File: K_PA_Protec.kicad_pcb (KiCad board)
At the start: 2 copper layers, 102.5 x 75 mm, 89 parts, among them IC1 MCP23017_SO, J1 IDC 10 Straight, J10 MH2, J11 MH3, J12 MH4, J13 MH5, J14 MH6, J2 Molex KK 4, J3 IDC 10 Straight, J4 Molex KK 2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

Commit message: routing, first stage
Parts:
- added G***: LOGO, Mod:Fcu, F.Cu at (115.0, 88.3)
- moved C15 10.6 mm to (88.5, 111.0)
- moved C24 9.96 mm to (127.5, 112.5), turned to -90 degrees
- moved SW1 9.67 mm to (147.8, 116.0), turned to 90 degrees
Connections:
- J2 pad 3: Net-(J2-Pad3) -> Net-(SW1-PadS2)
- SW1 pad S1: Net-(J2-Pad3) -> GND
- SW1 pad S2: GND -> Net-(SW1-PadS2)
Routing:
- net GND: track 0.00 -> 38.9 mm
- net Net-(SW1-PadS2): track 0.00 -> 34.8 mm
- net +12V: track 0.00 -> 24.9 mm
- net Net-(J7-Pad1): track 0.00 -> 13.8 mm
- net +15V: track 0.00 -> 13.4 mm
- net Net-(C15-Pad1): track 0.00 -> 12.4 mm
- net Net-(SW1-Pad2B): track 0.00 -> 7.74 mm
- net Net-(SW1-Pad2A): track 0.00 -> 4.67 mm
- net Net-(L3-Pad1): track 0.00 -> 4.35 mm
- net Net-(L1-Pad1): track 0.00 -> 4.15 mm
- added copper zone on F.Cu, net GND

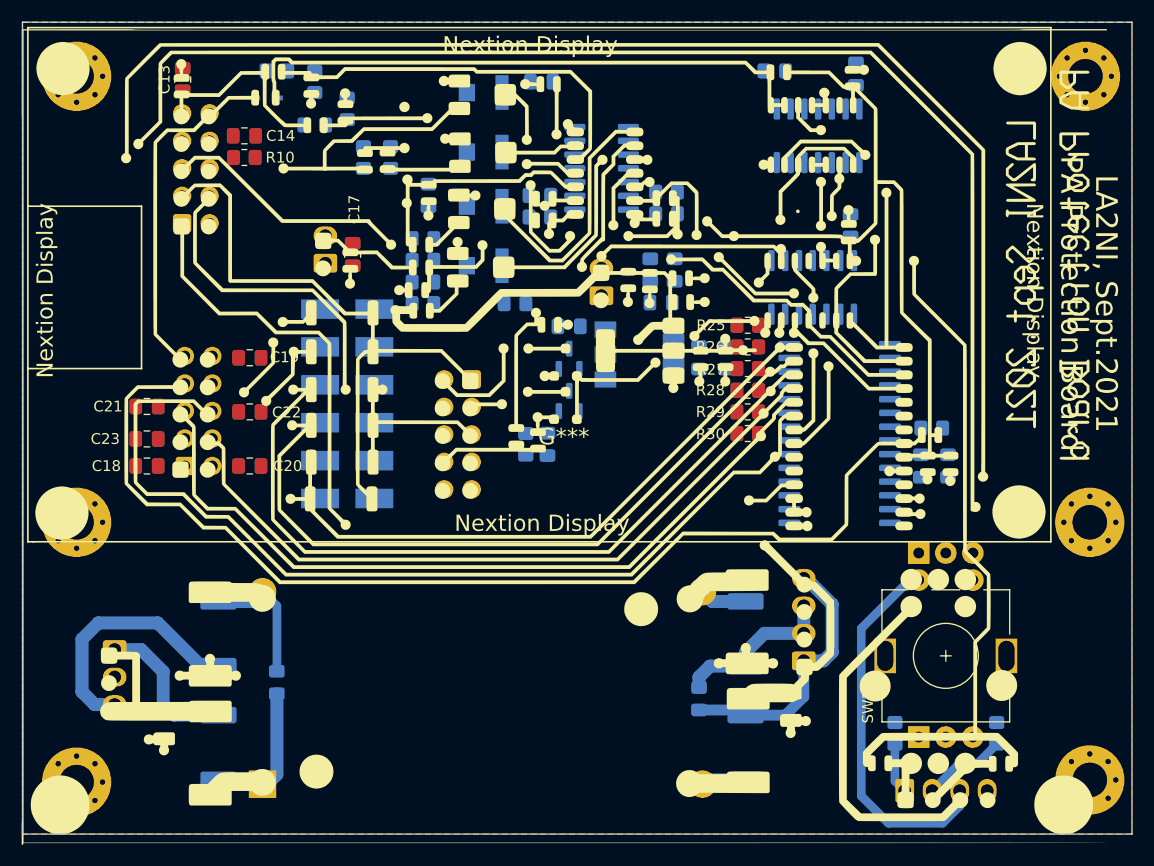
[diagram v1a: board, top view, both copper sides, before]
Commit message: routing completed, some minor changes expected
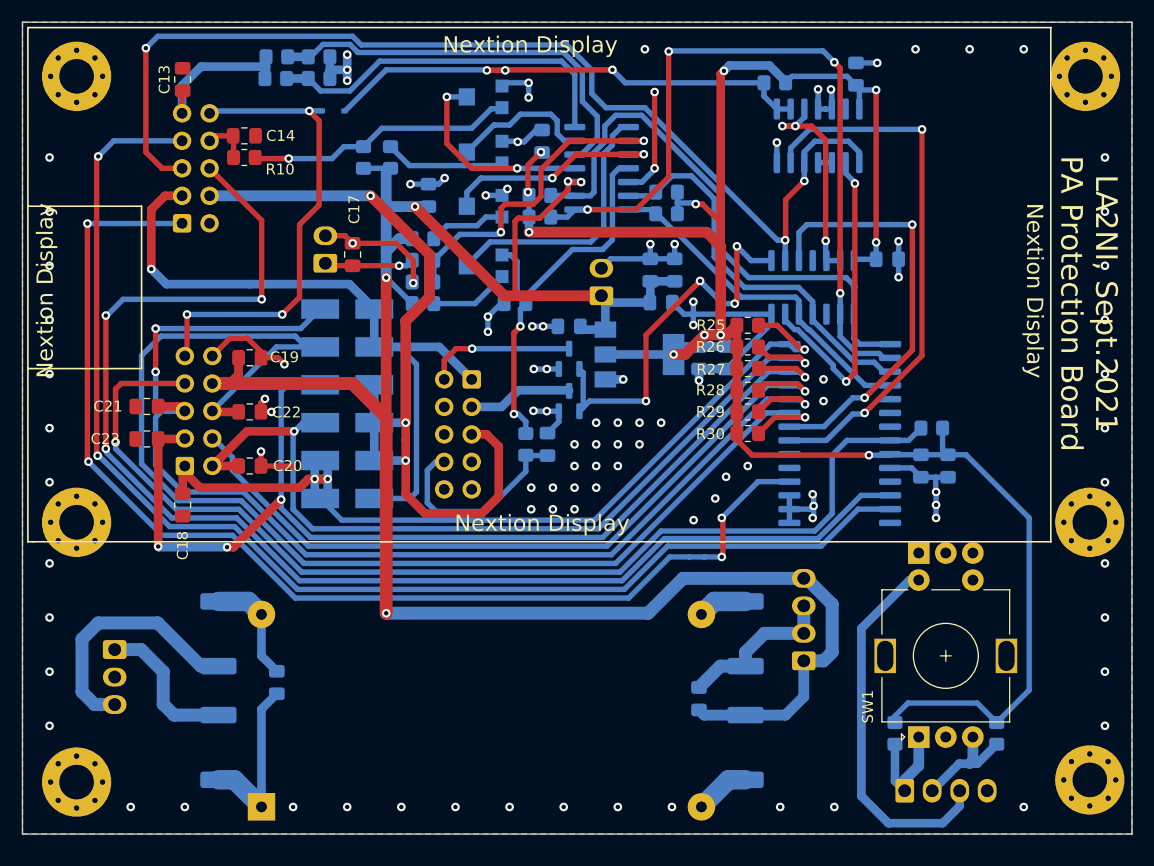
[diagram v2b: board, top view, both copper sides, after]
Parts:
- removed G***: LOGO, Mod:Fcu
- moved D1 6.12 mm to (93.7, 58.2)
- moved R11 5.61 mm to (88.4, 55.2)
- moved C2 5.50 mm to (113.0, 61.0), turned to 90 degrees
- moved C18 4.88 mm to (79.8, 94.6), turned to 90 degrees
- moved C9 4.60 mm to (144.9, 71.9), turned to 180 degrees
- moved R18 3.82 mm to (92.4, 55.2), turned to 180 degrees
- moved R22 2.33 mm to (92.4, 53.2), turned to 180 degrees
- moved U6 2.10 mm to (87.1, 122.5)
- moved R9 1.30 mm to (88.5, 53.2)
- moved R21 1.10 mm to (134.5, 55.6)
- moved RV12 0.40 mm to (107.5, 56.9)
- turned R17 to 0 degrees
- turned R20 to 0 degrees
- turned R24 to 90 degrees
- turned R6 to -90 degrees
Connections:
- C4 pad 2: Net-(C4-Pad2) -> +3V3
- C5 pad 2: Net-(C4-Pad2) -> +3V3
- J2 pad 1: Net-(SW1-Pad2A) -> Net-(J2-Pad1)
- J2 pad 2: Net-(SW1-Pad2B) -> Net-(J2-Pad2)
- R23 pad 2: Net-(SW1-Pad2A) -> Net-(J2-Pad1)
- R5 pad 2: Net-(SW1-Pad2B) -> Net-(J2-Pad2)
- SW1 pad 1A: (no net) -> unconnected-(SW1-Pad1A)
- SW1 pad 1B: (no net) -> unconnected-(SW1-Pad1B)
- SW1 pad 1C: (no net) -> unconnected-(SW1-Pad1C)
- SW1 pad 2A: (no net) -> Net-(J2-Pad1)
- SW1 pad 2B: (no net) -> Net-(J2-Pad2)
- SW1 pad 2C: (no net) -> GND
- U3 pad 1: Net-(IC1-Pad4) -> Net-(IC1-Pad1)
- U3 pad 2: Net-(IC1-Pad3) -> Net-(IC1-Pad2)
- U3 pad 4: Net-(IC1-Pad2) -> Net-(IC1-Pad3)
- U3 pad 5: Net-(IC1-Pad1) -> Net-(IC1-Pad4)
- U4 pad 2: Net-(C4-Pad2) -> +3V3
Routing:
- net +3V3: track 0.00 -> 189.1 mm, vias 0 -> 11
- net +12V: track 24.9 -> 211.9 mm, vias 0 -> 5
- net GND: track 38.9 -> 176.7 mm, vias 0 -> 107
- net SCL: track 0.00 -> 122.1 mm, vias 0 -> 3
- net 10m: track 0.00 -> 118.5 mm, vias 0 -> 1
- net SDA: track 0.00 -> 117.5 mm, vias 0 -> 2
- net 15m: track 0.00 -> 110.5 mm, vias 0 -> 3
- net Reset: track 0.00 -> 107.4 mm, vias 0 -> 4
- net 40m: track 0.00 -> 101.0 mm, vias 0 -> 4
- net 6m: track 0.00 -> 99.9 mm, vias 0 -> 1
- net D8: track 0.00 -> 99.8 mm, vias 0 -> 3
- net 160m: track 0.00 -> 84.3 mm, vias 0 -> 3
- net 80m: track 0.00 -> 83.7 mm, vias 0 -> 2
- net D5B: track 0.00 -> 76.0 mm, vias 0 -> 3
- net 20m: track 0.00 -> 70.8 mm, vias 0 -> 1
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- added copper zone on B.Cu, net GND

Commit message: small layout mods
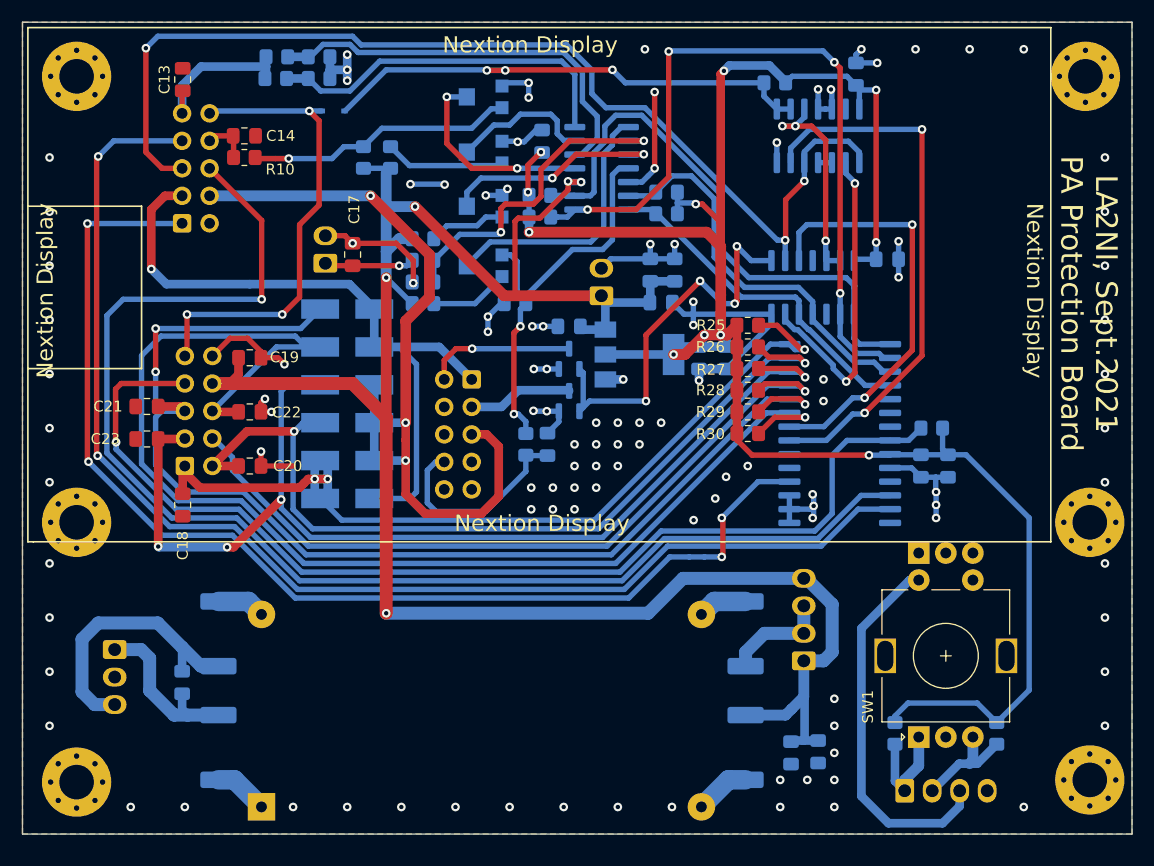
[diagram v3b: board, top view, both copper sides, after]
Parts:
- C15: value 100n -> 1u
- moved C1 62.8 mm to (138.5, 117.4), turned to 90 degrees
- moved C24 9.86 mm to (136.0, 117.5), turned to 90 degrees
- moved C15 8.75 mm to (79.8, 111.0)
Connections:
- C15 pad 1: Net-(C15-Pad1) -> GND
- C15 pad 2: +15V -> Net-(J7-Pad1)
- L4 pad 2: Net-(C15-Pad1) -> Net-(L4-Pad2)
- U6 pad 2: Net-(C15-Pad1) -> Net-(L4-Pad2)
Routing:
- net +15V: track 16.1 -> 5.02 mm
- net Net-(C15-Pad1): track 10.3 -> 0.00 mm
- net Net-(L4-Pad2): track 0.00 -> 4.48 mm
- net Net-(J7-Pad1): track 13.8 -> 16.0 mm
- net GND: track 176.7 -> 175.1 mm, vias 107 -> 114
- net +12V: track 211.9 -> 212.9 mm
- net SCL: track 122.1 -> 122.2 mm, vias 3 -> 1

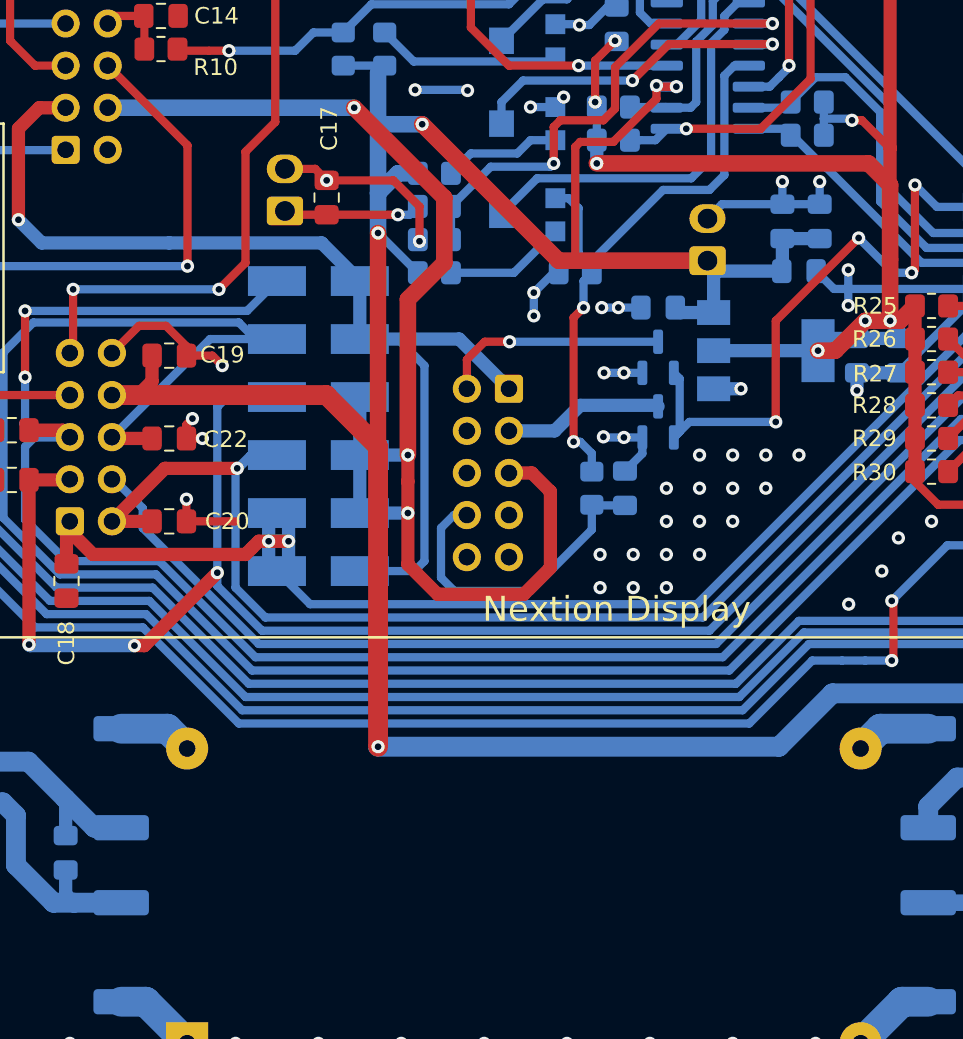
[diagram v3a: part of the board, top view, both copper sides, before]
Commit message: silkscreen cleanup, small routing mods
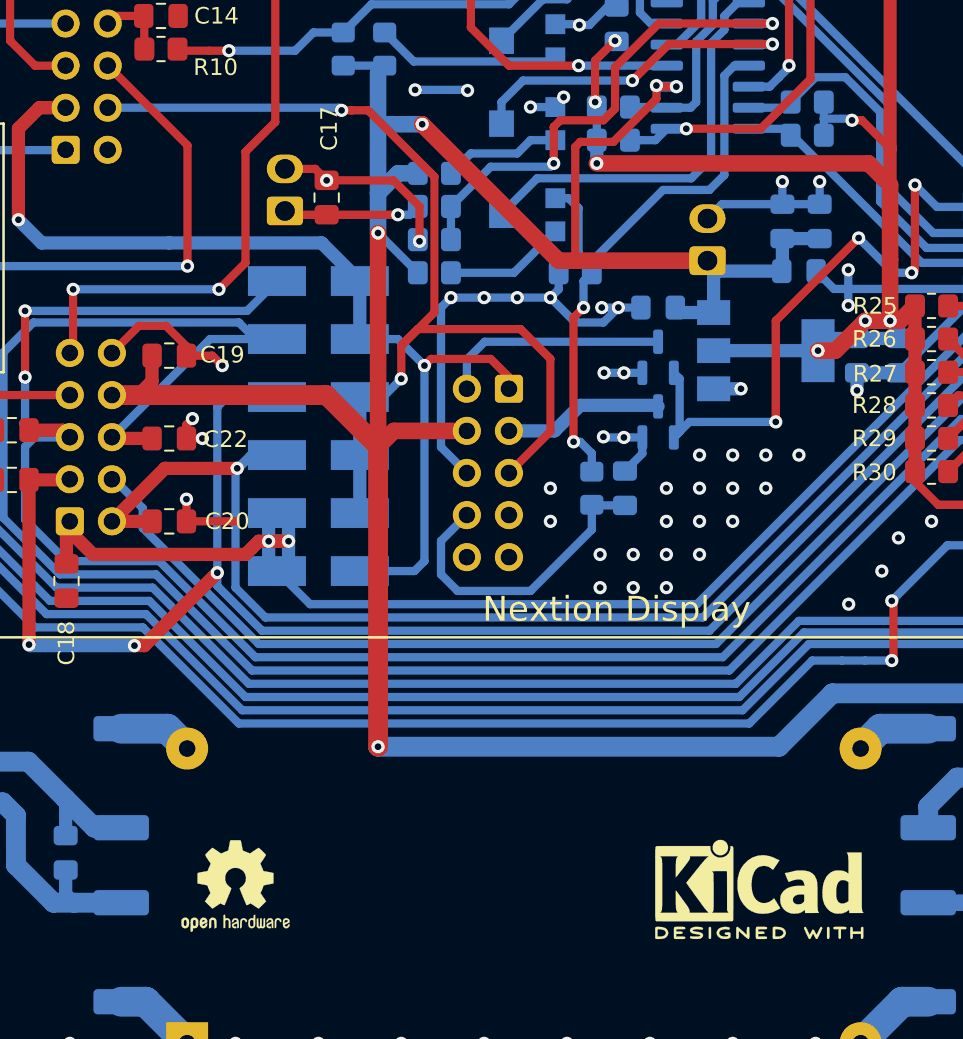
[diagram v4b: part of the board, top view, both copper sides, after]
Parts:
- added REF**: KiCad-Logo2_5mm_SilkScreen, Symbol:KiCad-Logo2_5mm_SilkScreen, F.Cu at (121.6, 113.2)
- added REF**: OSHW-Logo2_7.3x6mm_SilkScreen, Symbol:OSHW-Logo2_7.3x6mm_SilkScreen, F.Cu at (90.0, 113.0)
- added REF**: OSHW-Logo2_7.3x6mm_SilkScreen, Symbol:OSHW-Logo2_7.3x6mm_SilkScreen, B.Cu at (90.0, 113.0)
- added REF**: KiCad-Logo2_5mm_SilkScreen, Symbol:KiCad-Logo2_5mm_SilkScreen, B.Cu at (122.0, 113.2)
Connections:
- C1 pad 2: +12V -> +12V_A
- C11 pad 2: +12V -> +12V_A
- C12 pad 2: +12V -> +12V_A
- C19 pad 2: +12V -> +12V_A
- C24 pad 2: +12V -> +12V_A
- C3 pad 2: +12V -> +12V_A
- C6 pad 2: +12V -> +12V_A
- J5 pad 8: +12V -> +12V_A
- J6 pad 1: +12V -> +12V_A
- J8 pad 1: +12V -> +12V_A
- J8 pad 4: +12V -> +12V_A
- L1 pad 2: +12V -> +12V_A
- R24 pad 1: +12V -> +12V_A
- R6 pad 2: +12V -> +12V_A
- R7 pad 2: +12V -> +12V_A
- R8 pad 2: +12V -> +12V_A
- U1 pad 3: +12V -> +12V_A
- U4 pad 3: +12V -> +12V_A
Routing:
- net +12V_A: track 0.00 -> 218.6 mm, vias 0 -> 5
- net +12V: track 212.9 -> 0.00 mm, vias 5 -> 0
- net GND: track 175.1 -> 195.9 mm, vias 114 -> 118
- net D5B: track 76.0 -> 62.5 mm, vias 3 -> 2
- net D2A: track 62.7 -> 61.4 mm, vias 1 -> 2
- net DRV_PWR: track 19.4 -> 18.8 mm
- net RL2: vias 1 -> 0
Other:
- board text added: "+++"
- board text added: "++++"
- board text added: "12Vcc"
- board text added: "Ant Relay Board"
- board text added: "By f6itu"
- board text added: "DC Input 15-25V"
- board text added: "Encoder Out"
- board text added: "GND"
- board text added: "I/O Board"
- board text added: "Temp."
- board text added: "To Aries ATU"
- board text added: "To J16 on Aries ATU"

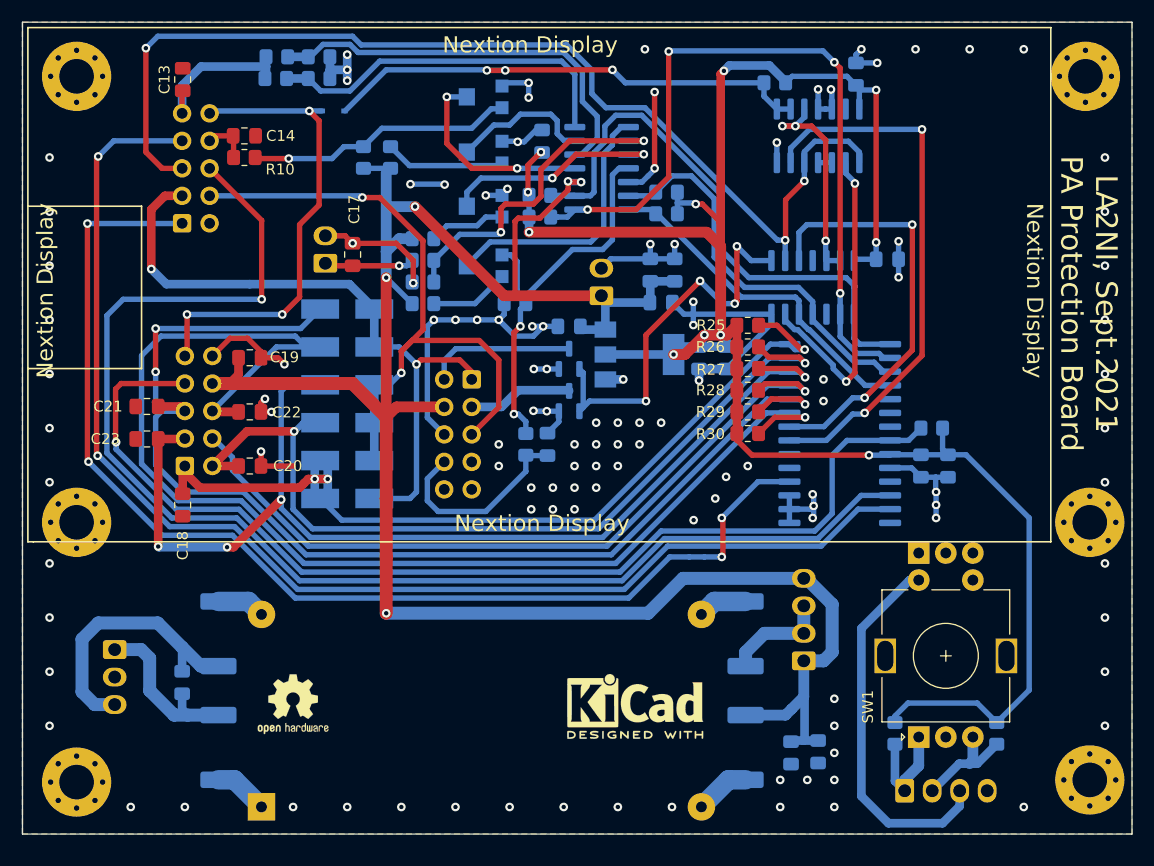
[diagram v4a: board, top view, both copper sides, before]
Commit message: nextion mounting holes fixed, last release before proto
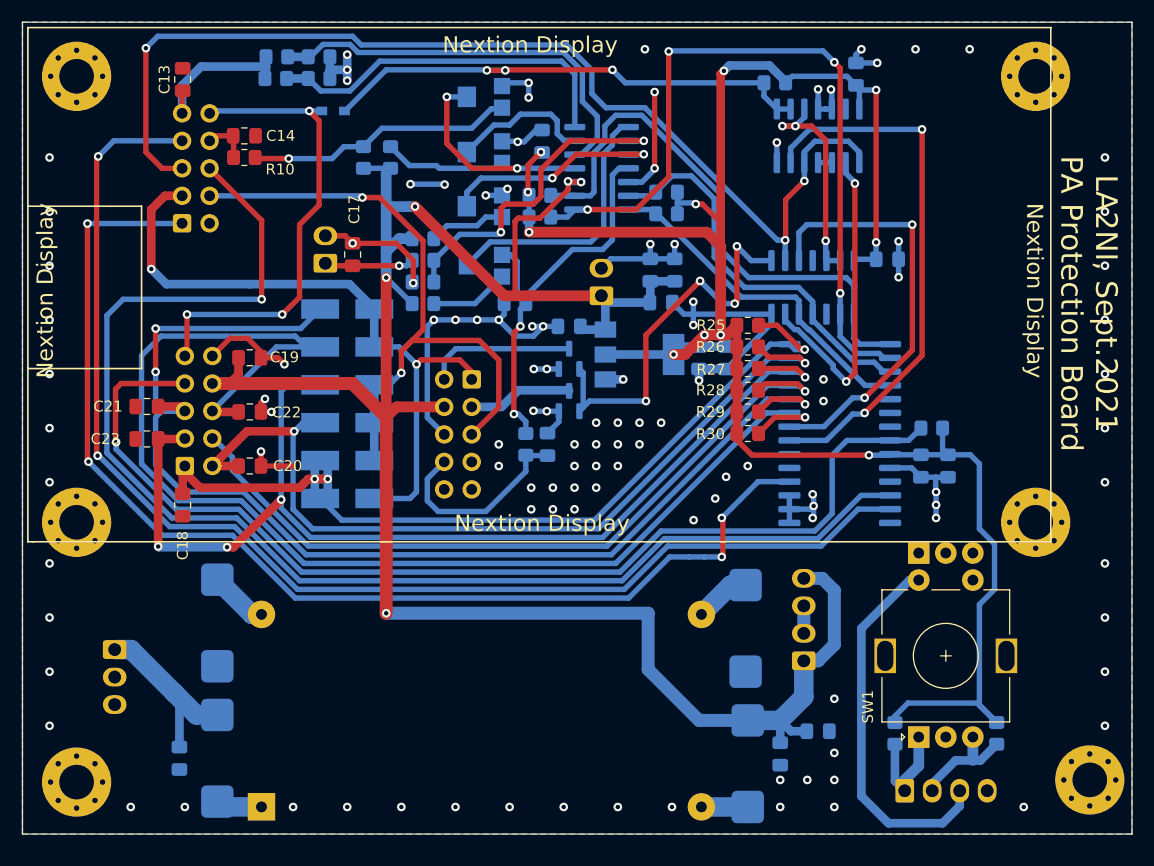
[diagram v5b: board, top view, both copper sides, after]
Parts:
- removed REF** (x2): KiCad-Logo2_5mm_SilkScreen, Symbol:KiCad-Logo2_5mm_SilkScreen
- removed REF** (x2): OSHW-Logo2_7.3x6mm_SilkScreen, Symbol:OSHW-Logo2_7.3x6mm_SilkScreen
- L1, L2, L3, L4: footprint Inductor_SMD:L_2512_6332Metric_Pad1.52x3.35mm_HandSolder -> Fair-Rite_2743021447:Fair-Rite_2743021447
- moved C15 7.00 mm to (79.5, 118.0), turned to 90 degrees
- moved J10 5.00 mm to (158.6, 96.2)
- moved J14 4.60 mm to (158.6, 55.0)
- moved C1 1.90 mm to (138.5, 115.5), turned to 180 degrees
- moved L1 1.51 mm to (132.0, 118.5)
- moved C24 1.00 mm to (135.0, 117.6)
- moved L2 1.00 mm to (83.0, 118.0)
- moved L4 1.00 mm to (83.0, 105.5)
- moved L3 0.50 mm to (131.8, 106.0)
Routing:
- net GND: track 195.9 -> 163.1 mm, vias 118 -> 116
- net Net-(C15-Pad2): track 16.0 -> 17.2 mm
- net +3V3: track 189.1 -> 188.0 mm
- net Net-(L4-Pad2): track 4.48 -> 5.41 mm
- net Net-(L1-Pad1): track 5.12 -> 4.28 mm
- net Net-(L3-Pad1): track 4.58 -> 5.40 mm
- net +15V: track 5.02 -> 4.28 mm

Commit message: minor changes in the README file
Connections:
- J7 pad 2: unconnected-(J7-Pad2) -> GND
- J7 pad 3: GND -> Net-(C15-Pad2)
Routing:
- net Net-(C15-Pad2): track 17.2 -> 23.1 mm

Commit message: Kicad 8.x file format
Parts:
- added REF**: KiCad-Logo2_5mm_SilkScreen, Symbol:KiCad-Logo2_5mm_SilkScreen, B.Cu at (154.5, 73.0)
- added REF**: OSHW-Logo2_7.3x6mm_SilkScreen, Symbol:OSHW-Logo2_7.3x6mm_SilkScreen, B.Cu at (162.0, 107.0)
